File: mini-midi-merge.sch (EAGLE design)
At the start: 66 parts, among them IC1 REG1117, X5 DIN5PIN

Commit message: almost done
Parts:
- removed LED6: (no value), led:LED3MM
- removed OK4: 6N138, optocoupler:6N138
- removed U$1: PIC16F1825SO14, jasons_stuff:PIC16F1825SO14
- removed U$8: 0805DIODE, jasons_stuff:0805DIODE
- added D1: 0805DIODE, jasons_stuff:0805DIODE
- added IC10: 6N138, optocoupler:6N138
- added IC5: REG1117, burr-brown:REG1117
- added L7: (no value), led:LED3MM
- IC1: value REG1117 -> PIC16F1825SO14; device burr-brown:REG1117 -> jasons_stuff:PIC16F1825SO14
- renumbered G1 to IC11, J1 to ICSP4, J2 to ICSP3, J3 to ICSP2, J4 to ICSP1, LED1 to L1, LED2 to L2, LED3 to L3, LED4 to L4, LED5 to L6, LED7 to L5, OK1 to IC9, OK2 to IC8, OK3 to IC7, U$2 to IC4, U$3 to IC3, U$4 to IC2, U$5 to D2, U$6 to D3, U$7 to D4
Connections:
- net GND: now also C1.1, C6.2, IC1.VSS, IC10.GND, IC5.GND, L7.C, R13.2, R15.2, R17.1, R18.2, R20.2, R22.1; no longer C1.2, C6.1, IC1.GND, LED6.C, OK4.GND, R13.1, R14.1, R2.2, R24.2, R5.2, R8.2, U$1.VSS
- net MIDI_IN0: now also IC1.RC5/RX, IC10.VO, R9.1; no longer OK4.VO, R12.1, U$1.RC5/RX
- net MIDI_IN1: now also R24.1; no longer R9.1
- net MIDI_IN2: now also R19.1; no longer R6.1
- net MIDI_IN3: now also R14.1; no longer R3.1
- net MIDI_OUT: now also IC1.RC4/TX, R1.1; no longer R16.1, U$1.RC4/TX
- net N$1: now also R16.1; no longer R1.1
- net N$10: now also R26.2; no longer R7.2
- net N$12: now also R25.1; no longer R8.1
- net N$13: now also R12.1; no longer R10.1
- net N$14: now also D1.P$2, IC10.A, R12.2; no longer OK4.A, R10.2, U$8.P$2
- net N$15: now also D1.P$1, IC10.C; no longer OK4.C, U$8.P$1
- net N$16: now also IC10.VB; no longer OK4.VB
- net N$17: now also R17.2; no longer R14.2
- net N$18: now also R22.2; no longer R13.2
- net N$19: now also R8.1; no longer R20.1
- net N$2: now also R16.2; no longer R1.2
- net N$20: now also C1.2, C8.+, IC5.VIN; no longer C5.2, C7.+, IC1.VIN
- net N$21: now also L7.A, R3.1; no longer LED6.A, R22.1
- net N$22: now also R1.2; no longer R16.2
- net N$26: now also R18.1; no longer R24.1
- net N$27: now also R10.2; no longer R15.2
- net N$28: now also R2.1; no longer R17.1
- net N$31: now also R13.1; no longer R25.1
- net N$32: now also IC1.RA3/MCLR#/VPP; no longer U$1.RA3/MCLR#/VPP
- net N$33: now also R4.1; no longer R21.1
- net N$34: now also IC1.RA0/ICSPDAT; no longer U$1.RA0/ICSPDAT
- net N$35: now also IC1.RA1/ICPCLK; no longer U$1.RA1/ICPCLK
- net N$36: now also IC1.RC2, R8.2; no longer R20.2, U$1.RC2
- net N$37: now also IC1.RA2/INT, R4.2; no longer R21.2, U$1.RA2/INT
- net N$4: now also R21.1; no longer R4.1
- net N$40: now also IC1.RA5; no longer U$1.RA5
- net N$41: now also IC1.RC3/SS#, R5.2; no longer R26.2, U$1.RC3/SS#
- net N$42: now also R5.1; no longer R26.1
- net N$5: now also R15.1; no longer R2.1
- net N$6: now also R21.2; no longer R4.2
- net N$8: now also R20.1; no longer R5.1
- net N$9: now also R26.1; no longer R7.1
- net SCL: now also IC1.RCO/SCL/SCK, R6.1; no longer R18.1, U$1.RCO/SCL/SCK
- net SDA: now also IC1.RC1/SDA/SDI, R7.1; no longer R19.1, U$1.RC1/SDA/SDI
- net VCC: now also C5.2, C6.1, C7.+, IC1.VDD, IC10.VCC, IC5.VOUT, R10.1, R14.2, R2.2, R24.2, R7.2; no longer C1.1, C6.2, C8.+, IC1.VOUT, OK4.VCC, R12.2, R15.1, R17.2, R18.2, R22.2, U$1.VDD
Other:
- moved on the sheet: C1, C2, C3, C4, C5, C6, C7, C8, IN, R1, R10, R11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

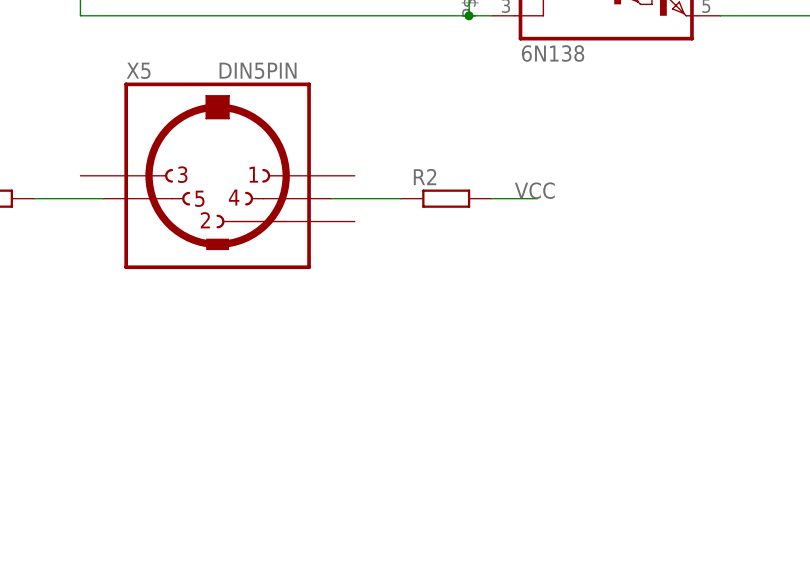
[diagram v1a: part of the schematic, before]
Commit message: ground output pin 2
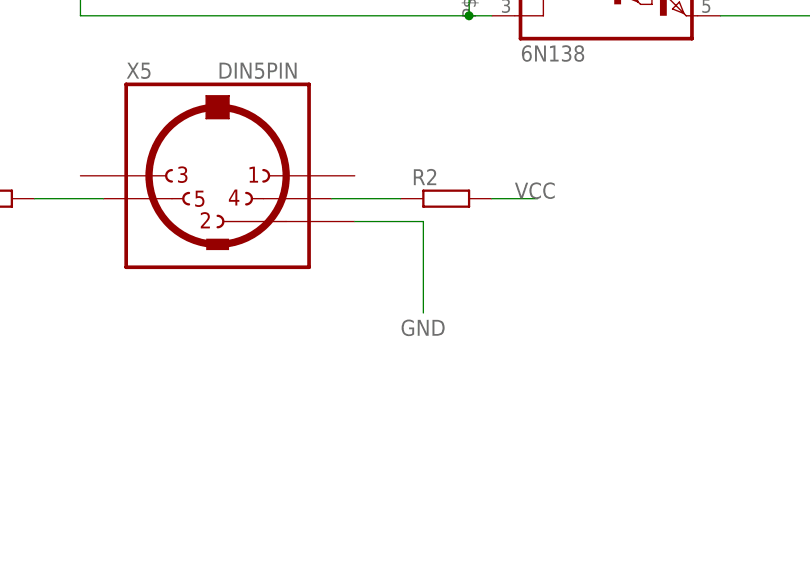
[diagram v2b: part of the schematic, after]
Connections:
- net GND: now also X5.2
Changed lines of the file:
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@@
 <label x="129.54" y="22.86" size="1.778" layer="95"/>
+</segment>
+<segment>
+<pinref part="X5" gate="G$1" pin="2"/>
+<wire x1="-7.62" y1="68.58" x2="0" y2="68.58" width="0.1524" layer="91"/>
+<wire x1="0" y1="68.58" x2="0" y2="58.42" width="0.1524" layer="91"/>
+<label x="-2.54" y="55.88" size="1.778" layer="95"/>
 </segment>
 </net>
